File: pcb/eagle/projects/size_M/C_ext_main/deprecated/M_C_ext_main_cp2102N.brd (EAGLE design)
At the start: 18 parts, among them U1 CP2104-F03-GM

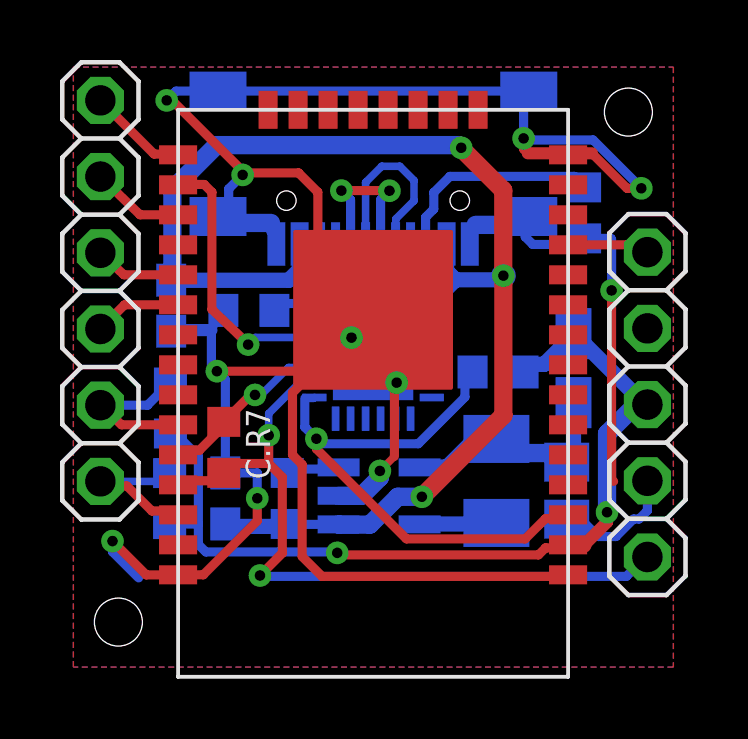
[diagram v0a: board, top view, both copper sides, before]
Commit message: version 8 main changes * ideal diode separated 3v3 DC-DC to protect it from back current * smaller package of ina 219 * usage of tssop attiny v2 in adapter * and change of PA5 to PB2 with ^ and ~ (originally used for shield power switch - now PB3) * step motor shield * out signal for BT module
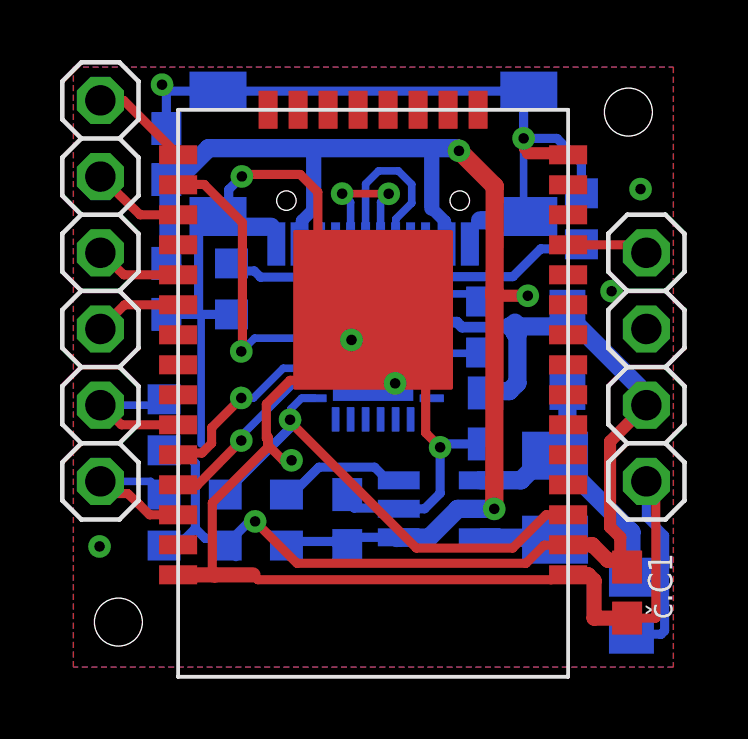
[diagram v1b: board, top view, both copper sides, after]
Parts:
- removed C.C2, C.C5: 4u7, rcl:C0603
- removed C.C3: 10u, rcl:C0805
- removed C.D1: SHOTKY_2.8, hugo:SHOTKY_2.8
- removed C.R1, C.R2: 2k2, rcl:R0603
- removed C.R3, C.R4: 100k, rcl:R0603
- removed C.R5: 5K1, rcl:R0603
- removed C.R6: 5k1, rcl:R0603
- removed C.R7: 4k7, rcl:R0603
- removed D.L1: 2u2, rcl:L3230M
- removed D.U2: LM3671_3.3, !stavebnice03:SOT32-5
- removed JP2: (no value), pinhead2:1X05
- removed U1: CP2104-F03-GM, CP2104:QFN50P400X400X80-25N
- added JP1: (no value), pinhead2:1X04
- added č.C1, č.C2, č.C4: 100n, rcl:C0603
- added č.C3: 10u, rcl:C0805
- added č.C5, č.C6: 4u7, rcl:C0603
- added č.D1: SHOTKY_2.8, hugo:SHOTKY_2.8
- added č.L1: 2u2, rcl:L3230M
- added č.R1, č.R2: 2k2, rcl:R0603
- added č.R3, č.R4, č.R8: 100k, rcl:R0603
- added č.R5: 5K1, rcl:R0603
- added č.R6: 5k1, rcl:R0603
- added č.U1: CP2102N, CP2104:QFN50P400X400X80-25N
- added č.U2: LM3671_3.3, !stavebnice03:SOT32-5
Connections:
- removed net N$15: C.U1.IO27, JP2.1
- new net N$16: č.R8.1, č.U1.9
- new net N$7: C.U1.IO27, JP1.1
- net GND: now also JP1.4, č.C1.2, č.C2.2, č.C3.2, č.C4.2, č.C5.1, č.C6.1, č.R5.1, č.R6.1, č.U1.2, č.U1.25, č.U2.GND; no longer C.C2.1, C.C3.2, C.C5.1, C.R5.1, C.R6.1, D.U2.GND, JP2.4, U1.2, U1.25
- net N$1: now also č.U1.4; no longer U1.4
- net N$10: now also č.L1.1, č.U2.VOUT; no longer D.L1.1, D.U2.VOUT
- net N$11: now also č.R3.1, č.U2.SHDN; no longer C.R3.1, D.U2.SHDN
- net N$2: now also č.U1.3; no longer U1.3
- net N$3: now also č.R6.2; no longer C.R6.2
- net N$4: now also č.R5.2; no longer C.R5.2
- net N$5: now also č.C3.1, č.D1.A, č.L1.2, č.U2.BP; no longer C.C3.1, C.D1.A, D.L1.2, D.U2.BP
- net N$8: now also č.R8.2, č.U1.5; no longer U1.5, U1.6
- net PROG: now also č.U1.23; no longer U1.23
- net RESET: now also č.R4.1, č.U1.19; no longer C.R4.1, U1.19
- net RX: now also č.U1.20; no longer C.R7.2, JP2.5, U1.20
- net SCL: now also č.R1.1; no longer C.R1.1
- net SDA: now also č.R2.1; no longer C.R2.1
- net TX: now also č.U1.21; no longer C.R7.1, U1.21
- net VCC: now also JP1.3, č.C1.1, č.C4.1, č.D1.K, č.R1.2, č.R2.2, č.R4.2, č.U1.6, č.U1.7; no longer C.D1.K, C.R1.2, C.R2.2, C.R4.2, JP2.3
- net VUSB: now also č.C2.1, č.C5.2, č.C6.2, č.R3.2, č.U2.VIN; no longer C.C2.2, C.C5.2, C.R3.2, D.U2.VIN, U1.7, U1.8
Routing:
- net RX: track 24.4 -> 6.06 mm, vias 2 -> 1
- net VCC: track 30.4 -> 42.1 mm, vias 2 -> 1
- net GND: track 122.7 -> 117.1 mm, vias 11 -> 10
- net N$5: track 8.01 -> 11.2 mm
- net VUSB: track 44.8 -> 41.7 mm
- net N$8: track 0.84 -> 3.76 mm
- net N$15: track 2.75 -> 0.00 mm
- net N$7: track 0.00 -> 2.72 mm
- net RESET: track 18.8 -> 16.3 mm
- net N$11: track 1.79 -> 4.34 mm
- net N$16: track 0.00 -> 1.70 mm
- net N$3: track 3.84 -> 4.65 mm
- net N$4: track 7.24 -> 6.56 mm
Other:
- board text added: "M8"
- board text added: "main2102N"
- board text removed: "main M.8"
